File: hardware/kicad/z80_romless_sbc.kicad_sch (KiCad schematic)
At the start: 51 parts, among them J1 REGULATED 5V INPUT, Q1 2N3904 MCP RESET, U1 Z84C0020PEC, U10 SN74LVC245AN bus-to-Pico, U2 AS6C1008-55PCN, U3 ATF22V10B/C, U4 SN74AHCT244N, U7 SN74LVC244AN, U8 MCP23S17-E/SP, U9 SN74AHCT245N Pico-to-bus

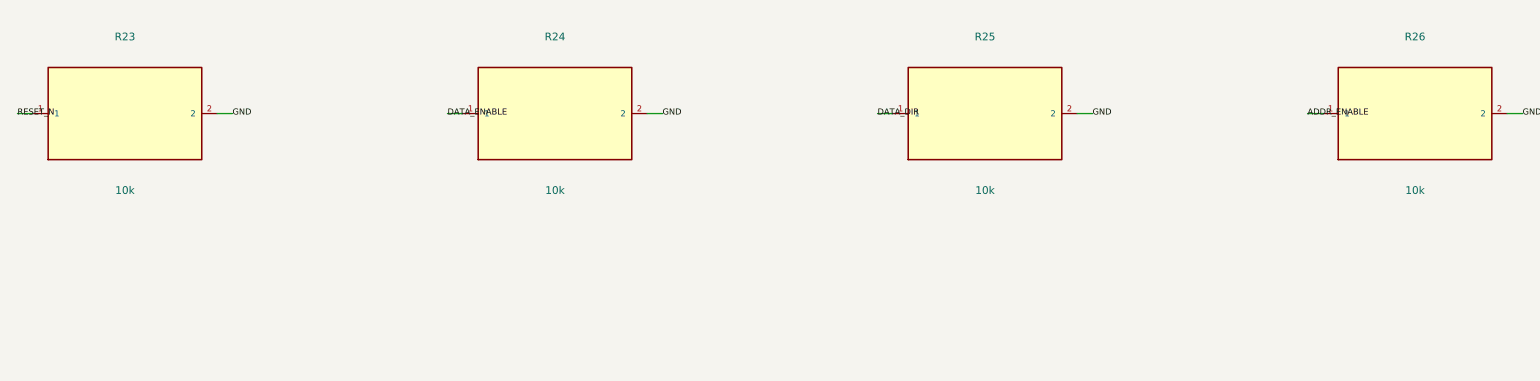
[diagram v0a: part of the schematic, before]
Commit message: Enhance PCB and schematic generation scripts, improve supervisor initialization, and expand test coverage
- Added +5V and GND assembly labels in build-kicad-pcb.py for better clarity.
- Updated build_board function to ensure correct layer settings for specific components.
- Implemented value checks for components in check_board function to ensure design integrity.
- Added checks for polarity silkscreen retention for capacitors C9 to C12.
- Modified resistor values in build-kicad-schematic.py based on signal requirements for improved circuit performance.
- Enhanced z80_safe_startup function in supervisor.c to initialize data pins correctly.
- Updated control_test to include supervisor.c for comprehensive testing.
- Expanded control_test.c with additional state tracking and assertions for safe startup and first write operations.
- Introduced sleep_ms function in fakes to simulate delays in tests.
- Included stdint.h in fakes/types.h for consistent type definitions.
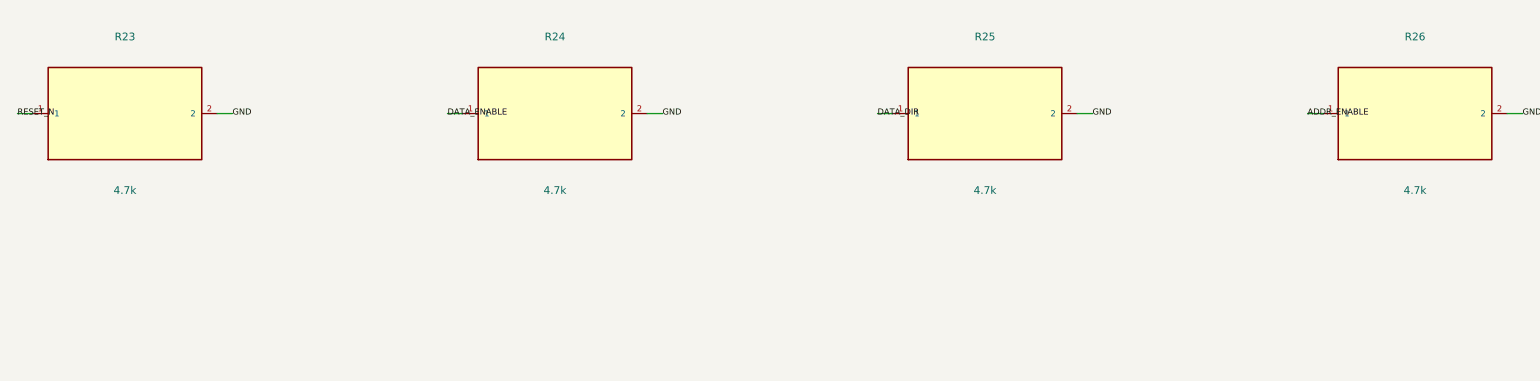
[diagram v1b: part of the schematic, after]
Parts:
- R23, R24, R25, R26: value 10k -> 4.7k

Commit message: Refactor Z80 SBC stages and tests
- Added loader tests for SRAM and CPU interactions in `loader_test.c`.
- Introduced stage 02 tests for buffer outputs in `stage02_test.c`.
- Removed obsolete SRAM control PLD file.
- Updated README for stage 00 to clarify testing procedures.
- Modified stage 01 supervisor to reflect changes in pin usage.
- Simplified stage 02 buffer clock management and command handling.
- Renamed stage 03 from MCP23S17 to control inputs, focusing on bus interactions.
- Streamlined stage 04 to emphasize CPU-driven address bus functionality.
- Adjusted stage 05 to focus on data transceivers without MCP23S17.
- Renamed stage 06 to reflect SRAM loader functionality.
- Updated stage 07 to enhance Z80 CPU execution and bus ownership.
- Refined stage 08 to improve virtual I/O handling.
- Revised stage 09 to focus on flash storage without MCP23S17.
- Enhanced stage 10 for WebSocket terminal interactions.
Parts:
- removed C12: 100u, Capacitor_THT:CP_Radial_D10.0mm_P5.00mm, symbol Z80SBC:CAPACITOR
- removed Q1: 2N3904 MCP RESET, Package_TO_SOT_THT:TO-92_Inline, symbol Z80SBC:NPN
- removed R24, R25, R26, R29: 4.7k, Resistor_THT:R_Axial_DIN0207_L6.3mm_D2.5mm_P10.16mm_Horizontal, symbol Z80SBC:RESISTOR
- removed R27, R28, R31: 10k, Resistor_THT:R_Axial_DIN0207_L6.3mm_D2.5mm_P10.16mm_Horizontal, symbol Z80SBC:RESISTOR
- removed R30: 47k, Resistor_THT:R_Axial_DIN0207_L6.3mm_D2.5mm_P10.16mm_Horizontal, symbol Z80SBC:RESISTOR
- removed RN5: 8x10k bussed, Resistor_THT:R_Array_SIP9, symbol Z80SBC:RN8
- removed U8: MCP23S17-E/SP, Package_DIP:DIP-28_W7.62mm, symbol Z80SBC:MCP23S17
- C11: value 22u -> 100u; footprint Capacitor_THT:CP_Radial_D8.0mm_P3.50mm -> Capacitor_THT:CP_Radial_D10.0mm_P5.00mm
- C8: value 100n -> 22u; footprint Capacitor_THT:C_Disc_D5.0mm_W2.5mm_P2.50mm -> Capacitor_THT:CP_Radial_D8.0mm_P3.50mm
- R23: value 4.7k -> 10k
- U3: value ATF22V10B/C -> SN74HCT32N; footprint Package_DIP:DIP-24_W7.62mm -> Package_DIP:DIP-14_W7.62mm; symbol Z80SBC:ATF22V10 -> Z80SBC:HCT32
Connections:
- net MCP_SCK is gone; now on net SRAM_CE_N: U4.12 (1Y4)
- net MCP_SI is gone; now on net SRAM_WE_N: U4.9 (2Y1)
- net MCP_SO is gone; now on net A0: U7.11 (2A1)
- net +3V3: now also C7.1 (+); no longer C8.1 (+), R21.2
- net +5V: now also C8.1 (+), U3.14 (VCC); no longer C7.1 (+), U3.24 (VCC)
- net A1: now also U7.13 (2A2)
- net A2: now also U7.15 (2A3)
- net A4: now also U7.17 (2A4)
- net BUSACK_N: no longer U3.2 (BUSACK#)
- net DATA_DOWN_OE_N: now also A1.10 (GP7), R20.1; no longer U3.18 (DATA_DOWN_OE#)
- net DATA_UP_OE_N: now also U3.8 (3Y); no longer U3.17 (DATA_UP_OE#)
- net GND: now also R21.2, U3.13 (4B), U3.7 (GND), U4.15 (2A3), U4.17 (2A4); no longer U7.13 (2A2), U7.15 (2A3), U7.17 (2A4)
- net IORQ_N: now also U3.4 (2A); no longer U3.13 (Z80_IORQ#)
- net MREQ_N: now also U4.8 (1A4); no longer U3.8 (Z80_MREQ#)
- net PICO_CLK: now also R21.1; no longer R22.1
- net RD_N: now also U3.9 (3A), U4.13 (2A2); no longer U3.6 (Z80_RD#)
- net RESET_N: now also R22.1; no longer R23.1, U3.1 (RESET#)
- net SRAM_CE_N: no longer U4.3 (2Y4)
- net SRAM_OE_N: now also U3.3 (1Y); no longer U4.5 (2Y3)
- net SRAM_WE_N: no longer U4.7 (2Y2)
- net WAIT_N: now also U3.6 (2Y); no longer U3.20 (WAIT#)
- net WR_N: now also U4.11 (2A1); no longer U3.4 (Z80_WR#)
- net PICO_A4: now reaches U7.3 (2Y4)
- net PICO_A4: now also A1.27 (GP21)
- net PICO_A2: now reaches U7.5 (2Y3)
- net PICO_A2: now also A1.26 (GP20)
- net PICO_A1: now reaches U7.7 (2Y2)
- net PICO_A1: now also A1.25 (GP19)
- net ADDR_ENABLE renamed IO_RELEASE
- net IO_RELEASE: now also R23.1, U3.5 (2B); no longer U3.10 (ADDR_ENABLE)
- net DATA_DIR: no longer names the net of U3.11 (4Y)
- net DATA_DIR: no longer A1.9 (GP6)
- removed net DATA_ENABLE: A1.10 (GP7), U3.9 (DATA_ENABLE)
- net MCP_CS_N renamed BOOT_READ_DISABLE_5V
- net BOOT_READ_DISABLE_5V: now also U3.2 (1B)
- removed net MCP_RESET_DRIVE: U3.19 (MCP_RESET_DRIVE)
- net PICO_CE_N renamed BOOT_READ_DISABLE
- net BOOT_READ_DISABLE: now also U4.6 (1A3); no longer U3.7 (PICO_CE#)
- removed net PICO_OE_N: A1.31 (GP26), R21.1, U3.5 (PICO_OE#)
- removed net PICO_SPI_CS_N: A1.27 (GP21), R19.1, U4.6 (1A3)
- net PICO_SPI_MISO renamed PICO_A0
- net PICO_A0: now also A1.24 (GP18); no longer A1.26 (GP20)
- removed net PICO_SPI_MOSI: A1.25 (GP19), U4.11 (2A1)
- removed net PICO_SPI_SCK: A1.24 (GP18), U4.8 (1A4)
- removed net PICO_WE_N: A1.29 (GP22), R20.1, U3.3 (PICO_WE#)
- removed net SRAM_CE_PRE_N: U3.16 (SRAM_CE_PRE#), U4.17 (2A4)
- removed net SRAM_OE_PRE_N: U3.15 (SRAM_OE_PRE#), U4.15 (2A3)
- removed net SRAM_WE_PRE_N: U3.14 (SRAM_WE_PRE#), U4.13 (2A2)
- new net PICO_DATA_UP_OE_N: A1.9 (GP6), R19.1, U3.10 (3B)
- new net RD_5V_N: U3.1 (1A), U4.7 (2Y2)
- no-connect marks 16 -> 13
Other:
- note added: "BOOT_CONTROL"
- note added: "BUFFERED_CONTROLS"
- note added: "CPU_TO_BUFFERS"
- note added: "PICO_TO_BUFFER"
- note added: "PORT_MONITOR"
- note added: "RN4: 5V control pull-ups. R17-R20: 3V3 pull-ups. R21-R23: GPIO pull-downs. Both data paths default disabled; no PLD/programmer required."
- note added: "Z80 is the sole SRAM address/write master. Pico injects instructions with SRAM reads inhibited. RESET_N directly joins Pico and Z80 at 3.3V."
- note removed: "ADDRESS_RESET"
- note removed: "CPU_TO_GAL"
- note removed: "GAL_TO_HCT"
- note removed: "HCT_TO_MCP"
- note removed: "Named KiCad buses show complete grouped routes; member pin stubs carry exact net labels. RESET_N is an explicit Pico / Z80 / GAL three-way wire junction."
- note removed: "PICO_TO_GAL"
- note removed: "PICO_TO_HCT"
- note removed: "RN4/RN5: 5V fail-safe pulls. R17-R21: 3V3 pulls. R22-R28: GPIO pull-downs. R29-R31: MCP reset transistor bias."

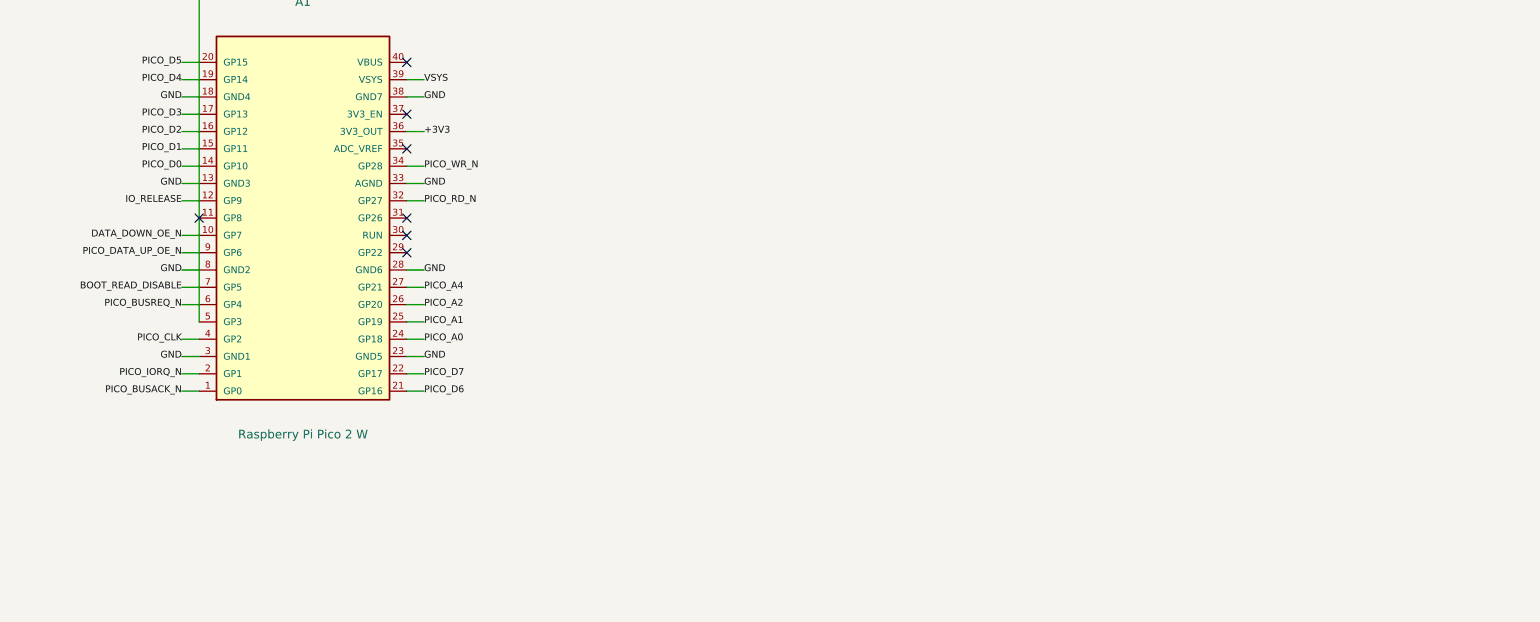
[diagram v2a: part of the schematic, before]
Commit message: Add PICO GPIO Expansion support to Z80 SBC schematic
- Introduced a new symbol "EXPANSION" in the KiCad schematic for the PICO GPIO expansion, including pins for GP8, GP22, GP26_ADC0, 3V3_OUT, and GND.
- Updated the build script to include the new expansion component with appropriate pin mappings and descriptions.
- Enhanced the documentation check script to validate connections for the new expansion header.
- Added a note in the schematic to clarify the usage of the GPIO expansion.
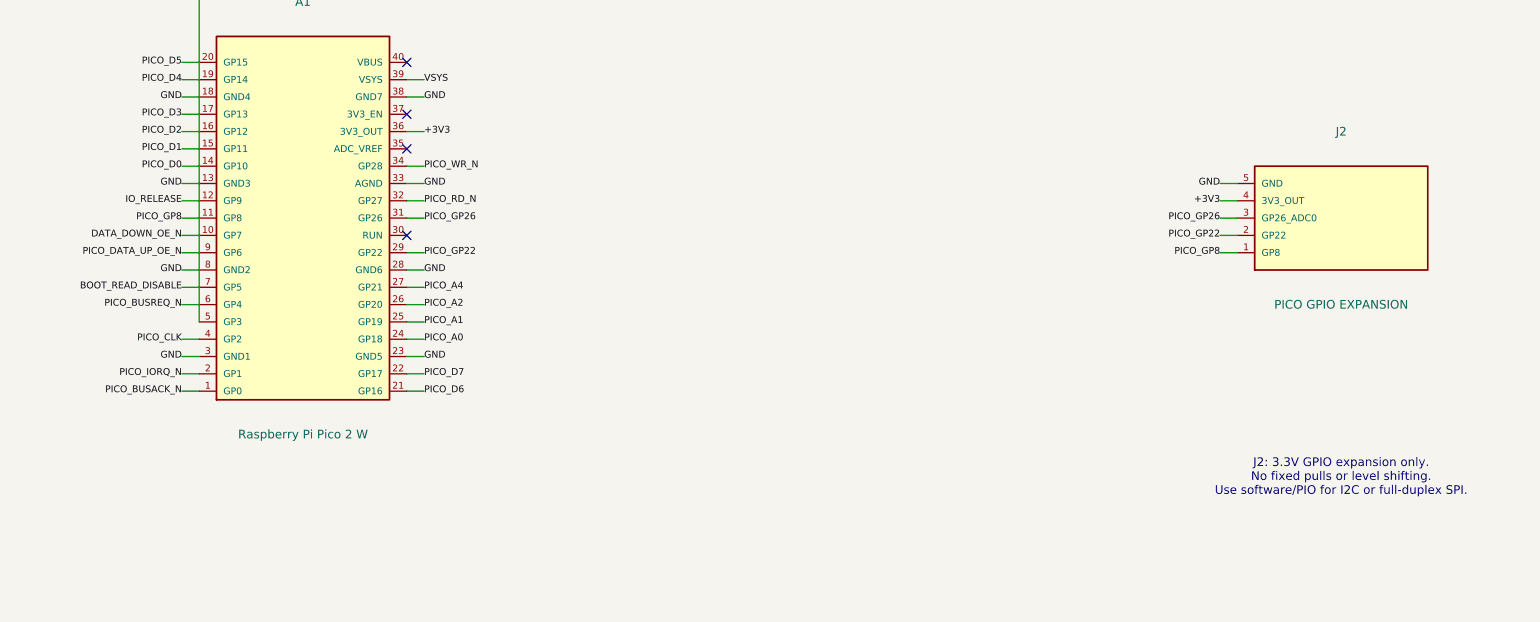
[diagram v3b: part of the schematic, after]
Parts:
- added J2: PICO GPIO EXPANSION, Connector_PinHeader_2.54mm:PinHeader_1x05_P2.54mm_Vertical, symbol Z80SBC:EXPANSION
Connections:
- net +3V3: now also J2.4 (3V3_OUT)
- net GND: now also J2.5 (GND)
- net PICO_GP8: now reaches A1.11 (GP8)
- net PICO_GP8: now also J2.1 (GP8)
- net PICO_GP22: now reaches A1.29 (GP22)
- net PICO_GP22: now also J2.2 (GP22)
- net PICO_GP26: now reaches A1.31 (GP26)
- net PICO_GP26: now also J2.3 (GP26_ADC0)
- no-connect marks 13 -> 10
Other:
- note added: "J2: 3.3V GPIO expansion only. No fixed pulls or level shifting. Use software/PIO for I2C or full-duplex SPI."
